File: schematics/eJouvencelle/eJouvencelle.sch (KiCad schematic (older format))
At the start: 9 parts

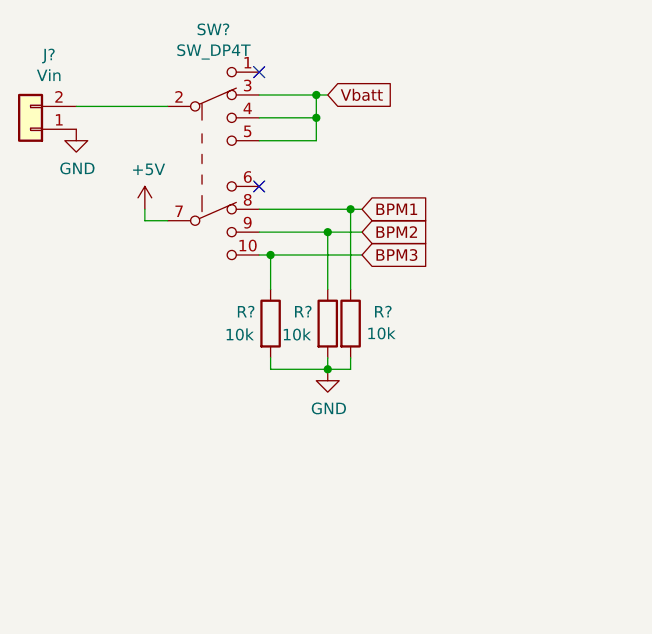
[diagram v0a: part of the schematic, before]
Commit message: square up main switch + text
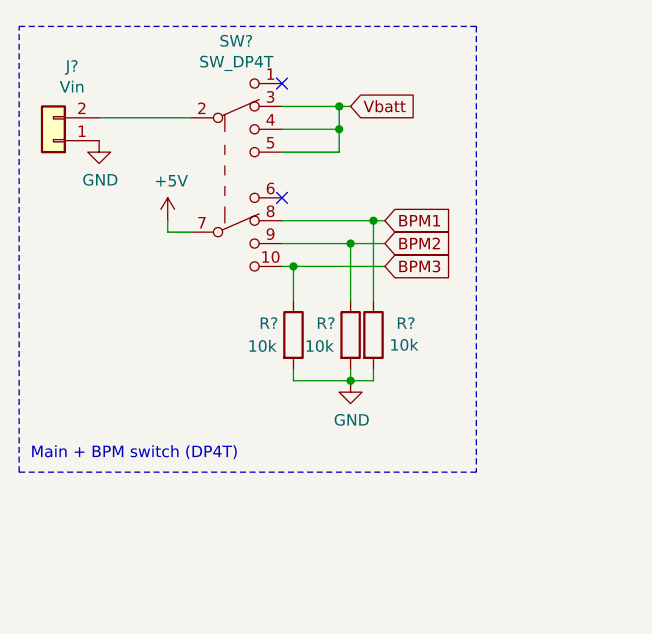
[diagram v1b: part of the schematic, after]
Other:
- note added: "Main + BPM switch (DP4T)"
- moved on the sheet: J?, R?, SW?
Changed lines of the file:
@@
 L eJouvencelle:SW_DP4T SW?
 U 1 1 5E8A8418
-P 1550 1200
-F 0 "SW?" H 1500 1785 50  0000 C CNN
-F 1 "SW_DP4T" H 1500 1694 50  0000 C CNN
-F 2 "" H 1450 1350 50  0001 C CNN
-F 3 "~" H 1450 1350 50  0001 C CNN
-	1    1550 1200
+P 1650 1250
+F 0 "SW?" H 1600 1835 50  0000 C CNN
+F 1 "SW_DP4T" H 1600 1744 50  0000 C CNN
+F 2 "" H 1550 1400 50  0001 C CNN
+F 3 "~" H 1550 1400 50  0001 C CNN
+	1    1650 1250
 	1    0    0    -1
 $EndComp
@@
 L Connector_Generic:Conn_01x02 J?
 U 1 1 5E8AB0B1
-P 700 1050
-F 0 "J?" H 618 725 50  0000 C CNN
-F 1 "Vin" H 618 816 50  0000 C CNN
-F 2 "" H 700 1050 50  0001 C CNN
-F 3 "~" H 700 1050 50  0001 C CNN
-	1    700  1050
+P 800 1100
+F 0 "J?" H 718 775 50  0000 C CNN
+F 1 "Vin" H 718 866 50  0000 C CNN
+F 2 "" H 800 1100 50  0001 C CNN
+F 3 "~" H 800 1100 50  0001 C CNN
+	1    800  1100
 	-1   0    0    1
 $EndComp
@@
 L power:GND #PWR?
 U 1 1 5E8AD4E2
-P 900 1050
-F 0 "#PWR?" H 900 800 50  0001 C CNN
-F 1 "GND" H 905 877 50  0000 C CNN
-F 2 "" H 900 1050 50  0001 C CNN
-F 3 "" H 900 1050 50  0001 C CNN
-	1    900  1050
+P 1000 1100
+F 0 "#PWR?" H 1000 850 50  0001 C CNN
+F 1 "GND" H 1005 927 50  0000 C CNN
+F 2 "" H 1000 1100 50  0001 C CNN
+F 3 "" H 1000 1100 50  0001 C CNN
+	1    1000 1100
 	1    0    0    -1
 $EndComp
 Wire Wire Line
-	900  950  1300 950
-NoConn ~ 1700 800
-NoConn ~ 1700 1300
-Text GLabel 2000 900  2    50   Input ~ 0
+	1000 1000 1400 1000
+NoConn ~ 1800 850
+NoConn ~ 1800 1350
+Text GLabel 2100 950  2    50   Input ~ 0
 Vbatt
 Wire Wire Line
-	1700 1000 1950 1000
+	1800 1050 2050 1050
 Wire Wire Line
-	1950 1000 1950 900
+	2050 1050 2050 950
 Wire Wire Line
-	1950 900  1700 900
+	2050 950  1800 950
 Wire Wire Line
-	1700 1100 1950 1100
+	1800 1150 2050 1150
 Wire Wire Line
-	1950 1100 1950 1000
-Connection ~ 1950 1000
+	2050 1150 2050 1050
+Connection ~ 2050 1050
 Wire Wire Line
-	2000 900  1950 900
-Connection ~ 1950 900
+	2100 950  2050 950
+Connection ~ 2050 950
 $Comp
 L power:+5V #PWR?
 U 1 1 5E8B2017
-P 1200 1400
-F 0 "#PWR?" H 1200 1250 50  0001 C CNN
-F 1 "+5V" H 1215 1573 50  0000 C CNN
-F 2 "" H 1200 1400 50  0001 C CNN
-F 3 "" H 1200 1400 50  0001 C CNN
-	1    1200 1400
+P 1300 1450
+F 0 "#PWR?" H 1300 1300 50  0001 C CNN
+F 1 "+5V" H 1315 1623 50  0000 C CNN
+F 2 "" H 1300 1450 50  0001 C CNN
+F 3 "" H 1300 1450 50  0001 C CNN
+	1    1300 1450
 	1    0    0    -1
 $EndComp
 Wire Wire Line
-	1200 1400 1200 1450
+	1300 1450 1300 1500
 Wire Wire Line
-	1200 1450 1300 1450
-Text GLabel 2150 1400 2    50   Input ~ 0
+	1300 1500 1400 1500
+Text GLabel 2250 1450 2    50   Input ~ 0
 BPM1
-Text GLabel 2150 1500 2    50   Input ~ 0
+Text GLabel 2250 1550 2    50   Input ~ 0
 BPM2
-Text GLabel 2150 1600 2    50   Input ~ 0
+Text GLabel 2250 1650 2    50   Input ~ 0
 BPM3
 $Comp
 L Device:R R?
 U 1 1 5E8B44F5
-P 1750 1900
-F 0 "R?" H 1600 1950 50  0000 L CNN
-F 1 "10k" H 1550 1850 50  0000 L CNN
-F 2 "" V 1680 1900 50  0001 C CNN
-F 3 "~" H 1750 1900 50  0001 C CNN
-	1    1750 1900
+P 1850 1950
+F 0 "R?" H 1700 2000 50  0000 L CNN
+F 1 "10k" H 1650 1900 50  0000 L CNN
+F 2 "" V 1780 1950 50  0001 C CNN
+F 3 "~" H 1850 1950 50  0001 C CNN
+	1    1850 1950
 	1    0    0    -1
 $EndComp
@@
 L Device:R R?
 U 1 1 5E8B514B
-P 2000 1900
-F 0 "R?" H 1850 1950 50  0000 L CNN
-F 1 "10k" H 1800 1850 50  0000 L CNN
-F 2 "" V 1930 1900 50  0001 C CNN
-F 3 "~" H 2000 1900 50  0001 C CNN
-	1    2000 1900
+P 2100 1950
+F 0 "R?" H 1950 2000 50  0000 L CNN
+F 1 "10k" H 1900 1900 50  0000 L CNN
+F 2 "" V 2030 1950 50  0001 C CNN
+F 3 "~" H 2100 1950 50  0001 C CNN
+	1    2100 1950
 	1    0    0    -1
 $EndComp
@@
 L Device:R R?
 U 1 1 5E8B5557
-P 2100 1900
-F 0 "R?" H 2200 1950 50  0000 L CNN
-F 1 "10k" H 2170 1855 50  0000 L CNN
-F 2 "" V 2030 1900 50  0001 C CNN
-F 3 "~" H 2100 1900 50  0001 C CNN
-	1    2100 1900
+P 2200 1950
+F 0 "R?" H 2300 2000 50  0000 L CNN
+F 1 "10k" H 2270 1905 50  0000 L CNN
+F 2 "" V 2130 1950 50  0001 C CNN
+F 3 "~" H 2200 1950 50  0001 C CNN
+	1    2200 1950
 	1    0    0    -1
 $EndComp
 Wire Wire Line
-	1750 1750 1750 1600
+	1850 1800 1850 1650
 Wire Wire Line
-	1750 1600 1700 1600
+	1850 1650 1800 1650
 Wire Wire Line
-	2000 1750 2000 1500
+	2100 1800 2100 1550
 Wire Wire Line
-	2100 1750 2100 1400
+	2200 1800 2200 1450
 $Comp
 L power:GND #PWR?
 U 1 1 5E8BA2A4
-P 2000 2100
-F 0 "#PWR?" H 2000 1850 50  0001 C CNN
-F 1 "GND" H 2005 1927 50  0000 C CNN
-F 2 "" H 2000 2100 50  0001 C CNN
-F 3 "" H 2000 2100 50  0001 C CNN
-	1    2000 2100
+P 2100 2150
+F 0 "#PWR?" H 2100 1900 50  0001 C CNN
+F 1 "GND" H 2105 1977 50  0000 C CNN
+F 2 "" H 2100 2150 50  0001 C CNN
+F 3 "" H 2100 2150 50  0001 C CNN
+	1    2100 2150
 	1    0    0    -1
 $EndComp
 Wire Wire Line
-	1750 2050 1750 2100
+	1850 2100 1850 2150
 Wire Wire Line
-	2100 2100 2100 2050
-Connection ~ 2000 2100
+	2200 2150 2200 2100
+Connection ~ 2100 2150
 Wire Wire Line
-	2000 2050 2000 2100
+	2100 2100 2100 2150
 Wire Wire Line
-	2150 1400 2100 1400
-Connection ~ 2100 1400
+	2250 1450 2200 1450
+Connection ~ 2200 1450
 Wire Wire Line
-	2150 1500 2000 1500
-Connection ~ 2000 1500
+	2250 1550 2100 1550
+Connection ~ 2100 1550
 Wire Wire Line
-	1700 1400 2100 1400
+	1800 1450 2200 1450
 Wire Wire Line
-	1700 1500 2000 1500
+	1800 1550 2100 1550
 Wire Wire Line
-	1750 1600 2150 1600
-Connection ~ 1750 1600
+	1850 1650 2250 1650
+Connection ~ 1850 1650
 Wire Wire Line
-	1750 2100 2000 2100
+	1850 2150 2100 2150
 Wire Wire Line
-	2100 2100 2000 2100
+	2200 2150 2100 2150
+Wire Notes Line
+	650  600  2650 600
+Wire Notes Line
+	2650 600  2650 2550
+Wire Notes Line
+	2650 2550 650  2550
+Wire Notes Line
+	650  2550 650  600
+Text Notes 700  2500 0    50   ~ 0
+Main + BPM switch (DP4T)
 $EndSCHEMATC

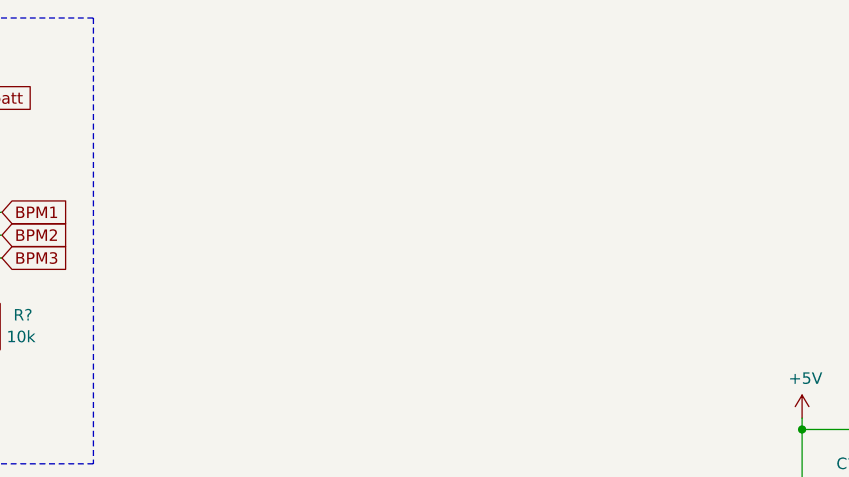
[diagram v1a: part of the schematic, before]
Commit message: add voltage regulator + rev voltage protection
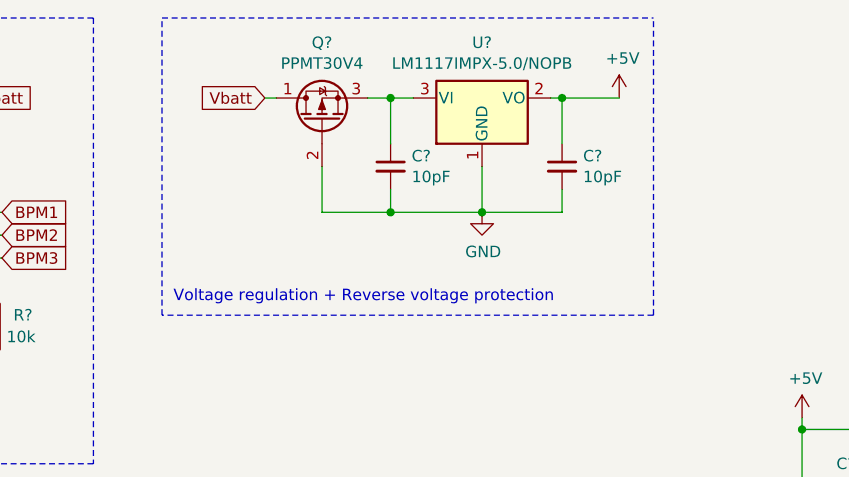
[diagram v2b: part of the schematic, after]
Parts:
- added C? (x2): 10pF, symbol Device:C_Small
- added Q?: PPMT30V4, symbol Device:Q_PMOS_DGS
- added U?: LM1117IMPX-5.0/NOPB, symbol Regulator_Linear:LM1117-5.0
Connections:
- net +5V: now also C?.1, U?.2 (VO)
- net GND: now also C?.2, C?.2, Q?.2 (G), U?.1 (GND)
- net Vbatt: now also Q?.1 (D)
- new net: C?.1, Q?.3 (S), U?.3 (VI)
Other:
- note added: "Voltage regulation + Reverse voltage protection"
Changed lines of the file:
@@
 Text Notes 700  2500 0    50   ~ 0
 Main + BPM switch (DP4T)
+$Comp
+L power:+5V #PWR?
+U 1 1 5E8E172E
+P 4950 950
+F 0 "#PWR?" H 4950 800 50  0001 C CNN
+F 1 "+5V" H 4965 1123 50  0000 C CNN
+F 2 "" H 4950 950 50  0001 C CNN
+F 3 "" H 4950 950 50  0001 C CNN
+	1    4950 950
+	1    0    0    -1
+$EndComp
+$Comp
+L power:GND #PWR?
+U 1 1 5E8E3004
+P 4350 1450
+F 0 "#PWR?" H 4350 1200 50  0001 C CNN
+F 1 "GND" H 4355 1277 50  0000 C CNN
+F 2 "" H 4350 1450 50  0001 C CNN
+F 3 "" H 4350 1450 50  0001 C CNN
+	1    4350 1450
+	1    0    0    -1
+$EndComp
+$Comp
+L Device:C_Small C?
+U 1 1 5E8E579B
+P 4700 1250
+F 0 "C?" H 4792 1296 50  0000 L CNN
+F 1 "10pF" H 4792 1205 50  0000 L CNN
+F 2 "" H 4700 1250 50  0001 C CNN
+F 3 "~" H 4700 1250 50  0001 C CNN
+	1    4700 1250
+	1    0    0    -1
+$EndComp
+Wire Wire Line
+	4350 1450 4700 1450
+Wire Wire Line
+	4700 1450 4700 1350
+Connection ~ 4350 1450
+Wire Wire Line
+	4700 1150 4700 950
+Wire Wire Line
+	4700 950  4650 950
+Connection ~ 4700 950
+Wire Wire Line
+	4350 1250 4350 1450
+$Comp
+L Regulator_Linear:LM1117-5.0 U?
+U 1 1 5E8E0075
+P 4350 950
+F 0 "U?" H 4350 1192 50  0000 C CNN
+F 1 "LM1117IMPX-5.0/NOPB" H 4350 1101 50  0000 C CNN
+F 2 "" H 4350 950 50  0001 C CNN
+F 3 "http://www.ti.com/lit/ds/symlink/lm1117.pdf" H 4350 950 50  0001 C CNN
+	1    4350 950
+	1    0    0    -1
+$EndComp
+$Comp
+L Device:Q_PMOS_DGS Q?
+U 1 1 5E8F175C
+P 3650 1050
+F 0 "Q?" V 3992 1050 50  0000 C CNN
+F 1 "PPMT30V4" V 3901 1050 50  0000 C CNN
+F 2 "" H 3850 1150 50  0001 C CNN
+F 3 "~" H 3650 1050 50  0001 C CNN
+	1    3650 1050
+	0    -1   -1   0
+$EndComp
+Wire Wire Line
+	3850 950  3950 950
+Wire Wire Line
+	3650 1250 3650 1450
+Wire Wire Line
+	3650 1450 3950 1450
+Text GLabel 3400 950  0    50   Input ~ 0
+Vbatt
+Wire Wire Line
+	3400 950  3450 950
+$Comp
+L Device:C_Small C?
+U 1 1 5E8F774D
+P 3950 1250
+F 0 "C?" H 4042 1296 50  0000 L CNN
+F 1 "10pF" H 4042 1205 50  0000 L CNN
+F 2 "" H 3950 1250 50  0001 C CNN
+F 3 "~" H 3950 1250 50  0001 C CNN
+	1    3950 1250
+	1    0    0    -1
+$EndComp
+Wire Wire Line
+	3950 1150 3950 950
+Connection ~ 3950 950
+Wire Wire Line
+	3950 950  4050 950
+Wire Wire Line
+	3950 1350 3950 1450
+Connection ~ 3950 1450
+Wire Wire Line
+	3950 1450 4350 1450
+Text Notes 3000 1850 0    50   ~ 0
+Voltage regulation + Reverse voltage protection
+Wire Notes Line
+	5100 1900 2950 1900
+Wire Notes Line
+	2950 1900 2950 600
+Wire Wire Line
+	4700 950  4950 950
+Wire Notes Line
+	5100 1900 5100 600
+Wire Notes Line
+	2950 600  5100 600
 $EndSCHEMATC

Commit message: add decoupling to AREF
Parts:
- added C?: 100pF, symbol Device:C_Small
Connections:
- net GND: now also C?.2
- net at U?.20 (AREF): now also C?.1
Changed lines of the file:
@@
 Wire Notes Line
 	2950 600  5100 600
+$Comp
+L Device:C_Small C?
+U 1 1 5E90CACE
+P 4900 3150
+F 0 "C?" H 4750 3200 50  0000 L CNN
+F 1 "100pF" H 4600 3150 50  0000 L CNN
+F 2 "" H 4900 3150 50  0001 C CNN
+F 3 "~" H 4900 3150 50  0001 C CNN
+	1    4900 3150
+	1    0    0    -1
+$EndComp
+$Comp
+L power:GND #PWR?
+U 1 1 5E90D7E6
+P 4900 3250
+F 0 "#PWR?" H 4900 3000 50  0001 C CNN
+F 1 "GND" H 4905 3077 50  0000 C CNN
+F 2 "" H 4900 3250 50  0001 C CNN
+F 3 "" H 4900 3250 50  0001 C CNN
+	1    4900 3250
+	1    0    0    -1
+$EndComp
+Wire Wire Line
+	5150 3050 4900 3050
 $EndSCHEMATC

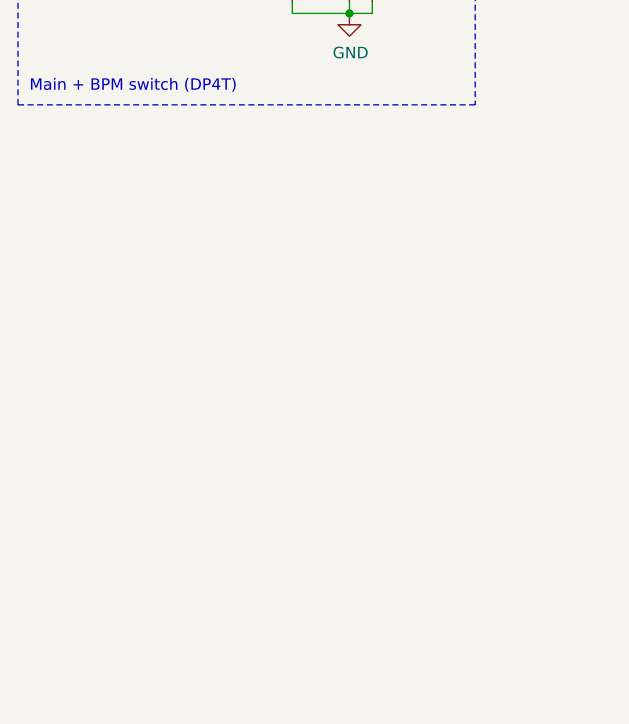
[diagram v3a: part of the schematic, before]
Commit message: add FTDI header
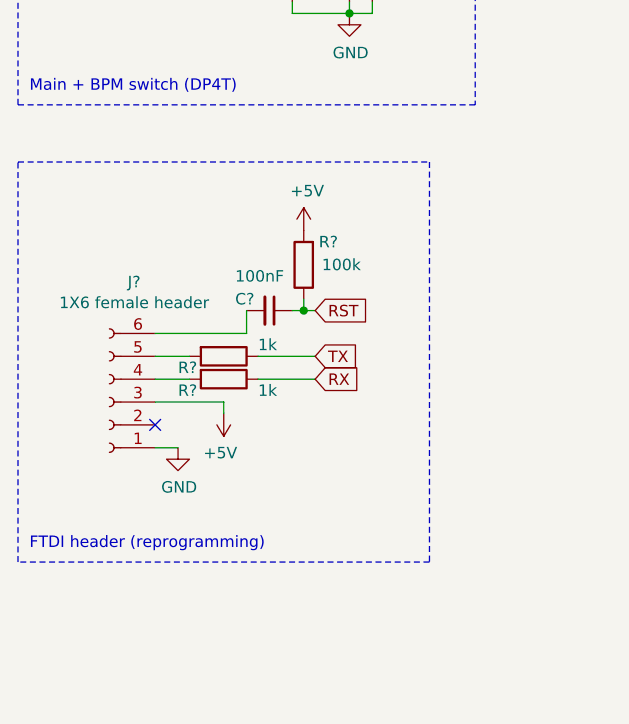
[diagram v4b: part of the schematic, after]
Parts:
- added C?: 100nF, symbol Device:C_Small
- added J?: 1X6 female header, symbol Connector:Conn_01x06_Female
- added R? (x2): 1k, symbol Device:R
- added R?: 100k, symbol Device:R
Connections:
- net +5V: now also J?.3 (Pin_3), R?.2
- net GND: now also J?.1 (Pin_1)
- new net: J?.4 (Pin_4), R?.2
- new net: J?.5 (Pin_5), R?.2
- new net: C?.2, J?.6 (Pin_6)
- new net RST: C?.1, R?.1
- new net RX: R?.1
- new net TX: R?.1
- no-connect marks 2 -> 3
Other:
- note added: "FTDI header (reprogramming)"
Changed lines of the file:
@@
 Wire Wire Line
 	5150 3050 4900 3050
+$Comp
+L Connector:Conn_01x06_Female J?
+U 1 1 5E912E98
+P 1050 3850
+F 0 "J?" H 942 3325 50  0000 C CNN
+F 1 "1X6 female header" H 942 3416 50  0000 C CNN
+F 2 "" H 1050 3850 50  0001 C CNN
+F 3 "~" H 1050 3850 50  0001 C CNN
+	1    1050 3850
+	-1   0    0    1
+$EndComp
+$Comp
+L power:GND #PWR?
+U 1 1 5E9155DD
+P 1350 4050
+F 0 "#PWR?" H 1350 3800 50  0001 C CNN
+F 1 "GND" H 1355 3877 50  0000 C CNN
+F 2 "" H 1350 4050 50  0001 C CNN
+F 3 "" H 1350 4050 50  0001 C CNN
+	1    1350 4050
+	1    0    0    -1
+$EndComp
+NoConn ~ 1250 3950
+$Comp
+L power:+5V #PWR?
+U 1 1 5E917405
+P 1550 3900
+F 0 "#PWR?" H 1550 3750 50  0001 C CNN
+F 1 "+5V" H 1565 4073 50  0000 C CNN
+F 2 "" H 1550 3900 50  0001 C CNN
+F 3 "" H 1550 3900 50  0001 C CNN
+	1    1550 3900
+	-1   0    0    1
+$EndComp
+$Comp
+L Device:R R?
+U 1 1 5E91C82E
+P 1550 3750
+F 0 "R?" V 1600 3550 50  0000 L CNN
+F 1 "1k" V 1600 3900 50  0000 L CNN
+F 2 "" V 1480 3750 50  0001 C CNN
+F 3 "~" H 1550 3750 50  0001 C CNN
+	1    1550 3750
+	0    1    1    0
+$EndComp
+$Comp
+L Device:R R?
+U 1 1 5E91D625
+P 1550 3650
+F 0 "R?" V 1600 3450 50  0000 L CNN
+F 1 "1k" V 1500 3800 50  0000 L CNN
+F 2 "" V 1480 3650 50  0001 C CNN
+F 3 "~" H 1550 3650 50  0001 C CNN
+	1    1550 3650
+	0    1    1    0
+$EndComp
+$Comp
+L Device:C_Small C?
+U 1 1 5E91D857
+P 1750 3450
+F 0 "C?" V 1700 3300 50  0000 L CNN
+F 1 "100nF" V 1600 3300 50  0000 L CNN
+F 2 "" H 1750 3450 50  0001 C CNN
+F 3 "~" H 1750 3450 50  0001 C CNN
+	1    1750 3450
+	0    1    1    0
+$EndComp
+Wire Wire Line
+	1350 4050 1250 4050
+Wire Wire Line
+	1550 3900 1550 3850
+Wire Wire Line
+	1550 3850 1250 3850
+Wire Wire Line
+	1400 3650 1250 3650
+Wire Wire Line
+	1400 3750 1250 3750
+Text GLabel 1950 3650 2    50   Input ~ 0
+TX
+Wire Wire Line
+	1950 3650 1700 3650
+Text GLabel 1950 3750 2    50   Input ~ 0
+RX
+Wire Wire Line
+	1950 3750 1700 3750
+Text GLabel 1950 3450 2    50   Input ~ 0
+RST
+Wire Wire Line
+	1250 3550 1650 3550
+Wire Wire Line
+	1650 3550 1650 3450
+$Comp
+L Device:R R?
+U 1 1 5E9329C4
+P 1900 3250
+F 0 "R?" H 1750 3150 50  0000 L CNN
+F 1 "100k" H 1650 3250 50  0000 L CNN
+F 2 "" V 1830 3250 50  0001 C CNN
+F 3 "~" H 1900 3250 50  0001 C CNN
+	1    1900 3250
+	-1   0    0    1
+$EndComp
+$Comp
+L power:+5V #PWR?
+U 1 1 5E933D66
+P 1900 3100
+F 0 "#PWR?" H 1900 2950 50  0001 C CNN
+F 1 "+5V" H 1915 3273 50  0000 C CNN
+F 2 "" H 1900 3100 50  0001 C CNN
+F 3 "" H 1900 3100 50  0001 C CNN
+	1    1900 3100
+	1    0    0    -1
+$EndComp
+Wire Wire Line
+	1900 3400 1900 3450
+Wire Wire Line
+	1900 3450 1850 3450
+Wire Wire Line
+	1950 3450 1900 3450
+Connection ~ 1900 3450
+Wire Notes Line
+	2450 2800 2450 4550
+Wire Notes Line
+	2450 4550 650  4550
+Wire Notes Line
+	650  4550 650  2800
+Wire Notes Line
+	650  2800 2450 2800
+Text Notes 700  4500 0    50   ~ 0
+FTDI header (reprogramming)
 $EndSCHEMATC
